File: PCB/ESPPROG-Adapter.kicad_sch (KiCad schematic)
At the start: 12 parts, among them J1 Conn_02x05_Odd_Even, J2 CONN ESP-PROG, J3 DebugHeader_Cortex-M_JTAG_10p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, J5 SOICBite connector UART Loopb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, J7 SOICBite IDC UART, J8 SOICBite connector numbering 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, J9 SOICBite IDC JTAG

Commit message: readme update
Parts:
- added JP1: ESPPROG_TX_RX_JUMP, Connector_PinHeader_2.54mm:PinHeader_2x03_P2.54mm_Vertical, symbol jmux-kicadlib:ESP-Prog-Adapter-Reversible-UART
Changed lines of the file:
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@@
+    )
+  )
+  (symbol (lib_id "jmux-kicadlib:ESP-Prog-Adapter-Reversible-UART") (at 112.522 37.846 0) (unit 1)
+    (in_bom yes) (on_board yes) (dnp no) (fields_autoplaced)
+    (property "Reference" "JP1" (at 112.522 30.48 0)
+      (effects (font (size 1.27 1.27)))
+    )
+    (property "Value" "ESPPROG_TX_RX_JUMP" (at 112.522 33.02 0)
+      (effects (font (size 1.27 1.27)))
+    )
+    (property "Footprint" "Connector_PinHeader_2.54mm:PinHeader_2x03_P2.54mm_Vertical" (at 113.792 46.736 0)
+      (effects (font (size 1.27 1.27)) hide)
+    )
+    (property "Datasheet" "" (at 112.522 37.846 0)
+      (effects (font (size 1.27 1.27)) hide)
+    )
+    (pin "4")
+    (pin "1")
+    (pin "5")
+    (pin "3")
+    (pin "2")
+    (pin "6")
+    (instances
+      (project "ESPPROG-Adapter"
+        (path "/0deeddec-331d-4e7e-80f3-64b8c983bbee"
+          (reference "JP1") (unit 1)
+        )
+      )
     )
   )
@@
         )
       )
+    )
+  )
+  (symbol (lib_id "jmux-kicadlib:ESP-Prog-Adapter-Reversible-UART") (at 111.252 55.118 0) (unit 2)
+    (in_bom yes) (on_board yes) (dnp no) (fields_autoplaced)
+    (property "Reference" "JP1" (at 111.252 46.99 0)
+      (effects (font (size 1.27 1.27)))
+    )
+    (property "Value" "ESPPROG_TX_RX_JUMP" (at 111.252 49.53 0)
+      (effects (font (size 1.27 1.27)))
+    )
+    (property "Footprint" "Connector_PinHeader_2.54mm:PinHeader_2x03_P2.54mm_Vertical" (at 112.522 64.008 0)
+      (effects (font (size 1.27 1.27)) hide)
+    )
+    (property "Datasheet" "" (at 111.252 55.118 0)
+      (effects (font (size 1.27 1.27)) hide)
+    )
+    (pin "4")
+    (pin "1")
+    (pin "5")
+    (pin "3")
+    (pin "2")
+    (pin "6")
+    (instances
+      (project "ESPPROG-Adapter"
+        (path "/0deeddec-331d-4e7e-80f3-64b8c983bbee"
+          (reference "JP1") (unit 2)
+        )
+      )

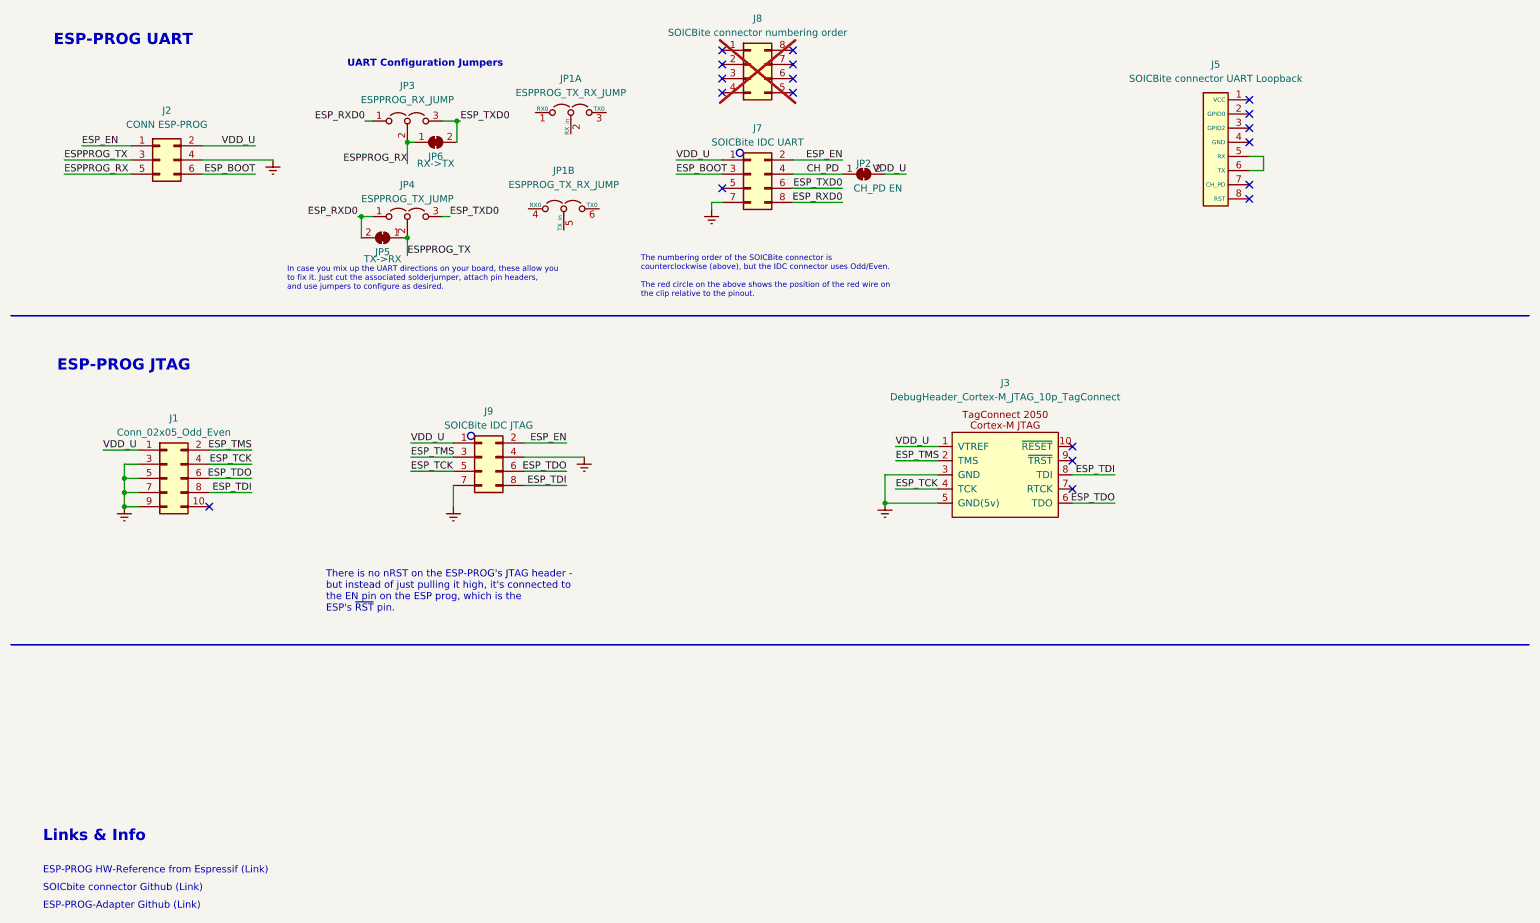
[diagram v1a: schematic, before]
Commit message: Writeup and minor changes for v1.4
v1.3 arrived and all functionality was confirmed working. This commit
adds the writeup, license, and some small modifications to the PCB to
make it a little easier to use.

* PCB updated to clarify assembly and use (text enlarged, dual 1x3 headers for reversible UART changed to single 2x3P using custom symbol).
* Vdd for JTAG and UART disconnected from each other on adapter, allowing different voltage to be used for each.
* Connected nRST line of ESP-PROG (from UART header) to board RESET line on JTAG pinout with solderjumper.
* Default connected solderjumpers changed to default open for Reversible UART, since I anticipate it'll be more used than not.
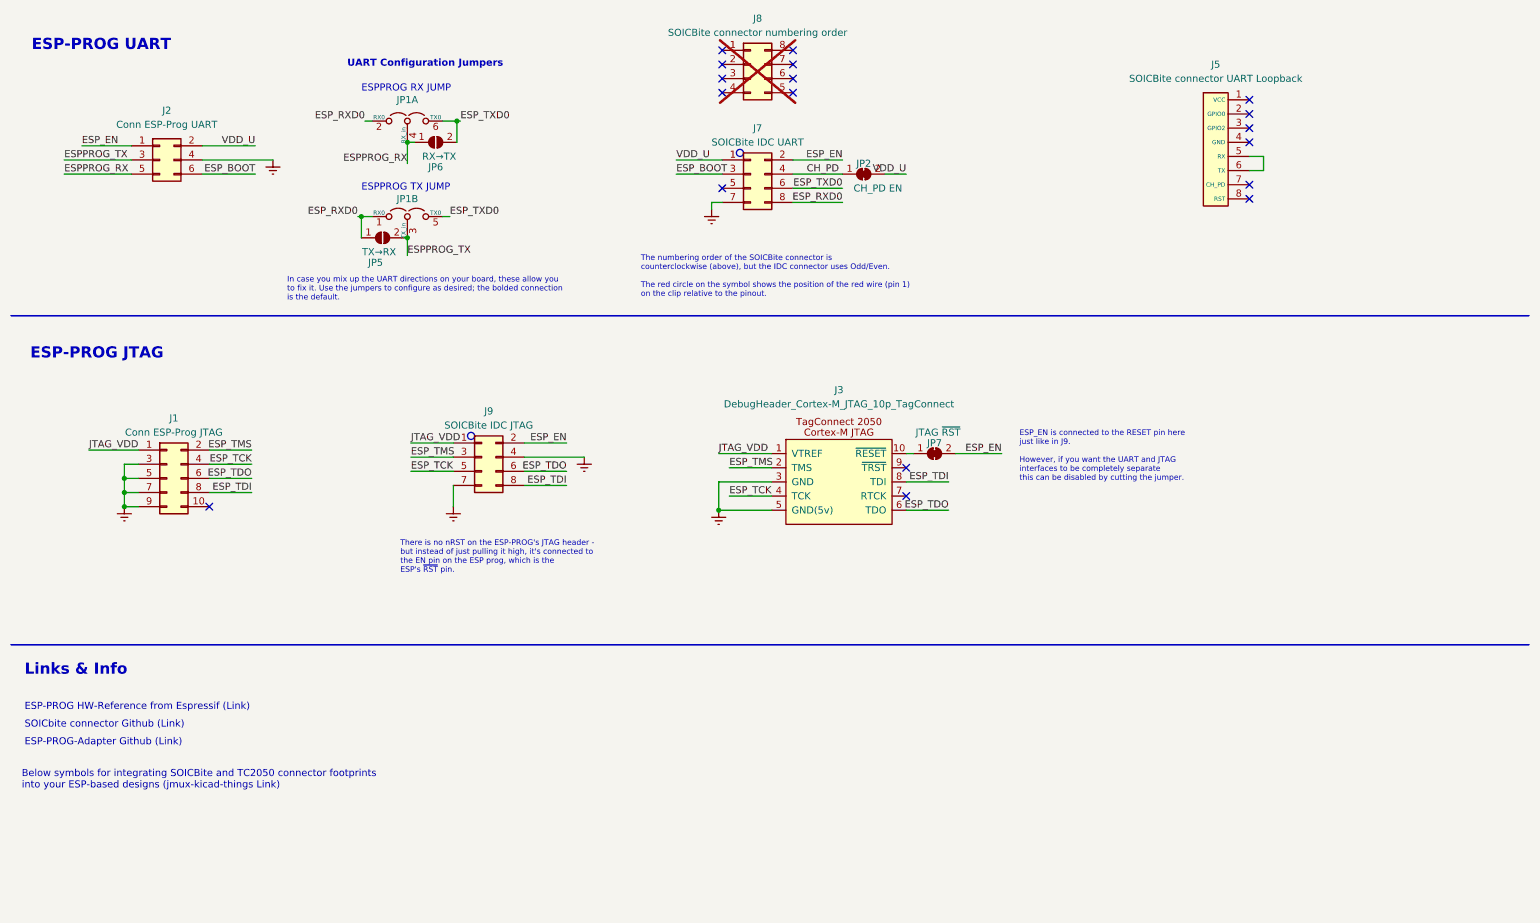
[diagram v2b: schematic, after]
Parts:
- removed JP3: ESPPROG_RX_JUMP, Connector_PinHeader_2.54mm:PinHeader_1x03_P2.54mm_Vertical, symbol Jumper:Jumper_3_Open
- removed JP4: ESPPROG_TX_JUMP, Connector_PinHeader_2.54mm:PinHeader_1x03_P2.54mm_Vertical, symbol Jumper:Jumper_3_Open
- removed JP5: TX->RX, Jumper:SolderJumper-2_P1.3mm_Bridged_RoundedPad1.0x1.5mm, symbol Jumper:SolderJumper_2_Bridged
- removed JP6: RX->TX, Jumper:SolderJumper-2_P1.3mm_Bridged_RoundedPad1.0x1.5mm, symbol Jumper:SolderJumper_2_Bridged
- added JP5: TX→RX, Jumper:SolderJumper-2_P1.3mm_Open_RoundedPad1.0x1.5mm, symbol Jumper:SolderJumper_2_Open
- added JP6: RX→TX, Jumper:SolderJumper-2_P1.3mm_Open_RoundedPad1.0x1.5mm, symbol Jumper:SolderJumper_2_Open
- added JP7: JTAG ~{RST}, Jumper:SolderJumper-2_P1.3mm_Bridged_RoundedPad1.0x1.5mm, symbol Jumper:SolderJumper_2_Bridged
- J1: value Conn_02x05_Odd_Even -> Conn ESP-Prog JTAG; LCSC (none) -> C18723056; Link (none) -> https://www.lcsc.com/product-detail/Female-Headers_HanElect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
- J2: value CONN ESP-PROG -> Conn ESP-Prog UART
- J3: Link (none) -> https://www.lcsc.com/product-detail/IDC-Connectors_XKB-Conn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
- J5, J8, JP2: LCSC (none) -> -
- JP1: LCSC (none) -> C2935918; Link (none) -> https://www.lcsc.com/product-detail/Pin-Headers_DEALON-DZ25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
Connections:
- net ESPPROG_RX: now also JP1.4 (RX_in), JP6.1 (A)
- net ESPPROG_TX: now also JP1.3 (TX_in), JP5.2 (B)
- net ESP_EN: now also JP7.2 (B)
- net ESP_RXD0: now also JP1.1 (RX0), JP1.2 (RX0), JP5.1 (A)
- net ESP_TXD0: now also JP1.5 (TX0), JP1.6 (TX0), JP6.2 (B)
- net VDD_U: no longer J1.1 (Pin_1), J3.1 (VTREF), J9.1 (Pin_1)
- net at J3.10 (~{RESET}): now also JP7.1 (A)
- new net JTAG_VDD: J1.1 (Pin_1), J3.1 (VTREF), J9.1 (Pin_1)
- no-connect marks 19 -> 18
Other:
- note added: "Below symbols for integrating SOICBite and TC2050 connector footprints into your ESP-based designs (jmux-kicad-things Link)"
- note added: "ESPPROG RX JUMP"
- note added: "ESPPROG TX JUMP"
- note added: "ESP_EN is connected to the RESET pin here just like in J9. However, if you want the UART and JTAG interfaces to be completely separate this can be disabled by cutting the jumper."
- note added: "In case you mix up the UART directions on your board, these allow you to fix it. Use the jumpers to configure as desired; the bolded connection is the default."
- note added: "The numbering order of the SOICBite connector is counterclockwise (above), but the IDC connector uses Odd/Even. The red circle on the symbol shows the position of the red wire (pin 1) on the clip relative to the pinout."
- note removed: "In case you mix up the UART directions on your board, these allow you to fix it. Just cut the associated solderjumper, attach pin headers, and use jumpers to configure as desired."
- note removed: "The numbering order of the SOICBite connector is counterclockwise (above), but the IDC connector uses Odd/Even. The red circle on the above shows the position of the red wire on the clip relative to the pinout."
- moved on the sheet: J3, JP1A, JP1B
